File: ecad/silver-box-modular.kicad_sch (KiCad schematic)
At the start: 16 parts, among them J1 B6B-XH-A(LF)(SN), U1 CD4051BPWR4, U2 ESP32-DevKitC-V4-32D-custom-p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

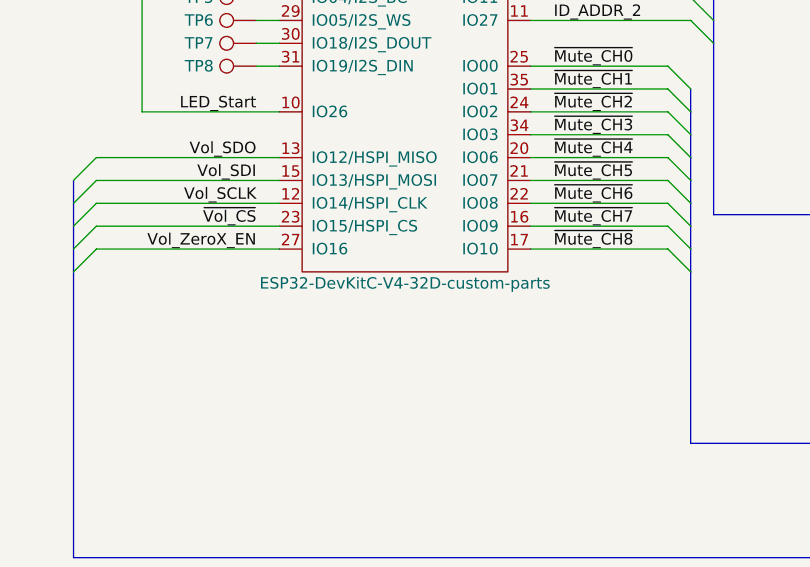
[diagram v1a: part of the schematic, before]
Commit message: Fixes to footprint numbering in multi-unit parts.
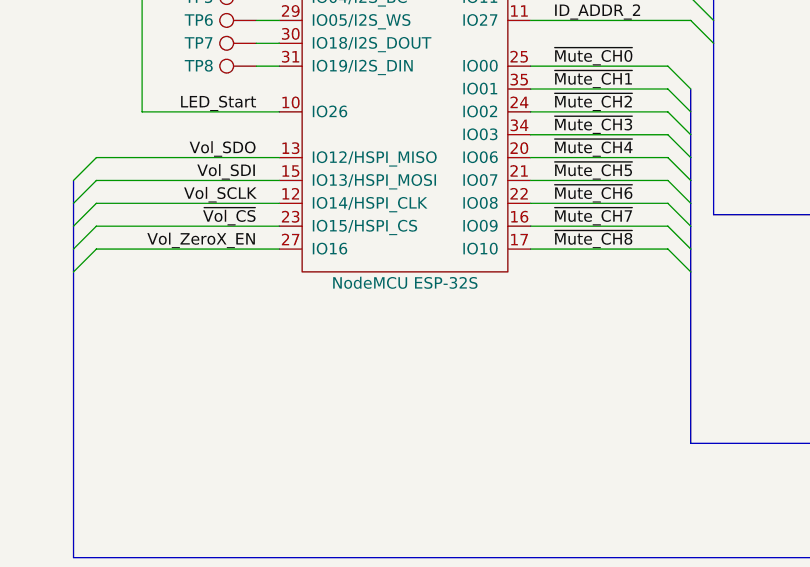
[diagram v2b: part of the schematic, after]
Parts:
- U2: value ESP32-DevKitC-V4-32D-custom-parts -> NodeMCU ESP-32S; footprint feetprints:ESP32-DevKitC-V4-32D -> silver-box-feetprints:NodeMCU ESP-32S
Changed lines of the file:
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@@
       (effects (font (size 1.27 1.27)))
     )
-    (property "Value" "ESP32-DevKitC-V4-32D-custom-parts" (at 148.59 177.8 0)
+    (property "Value" "NodeMCU ESP-32S" (at 148.59 177.8 0)
       (effects (font (size 1.27 1.27)))
     )
-    (property "Footprint" "feetprints:ESP32-DevKitC-V4-32D" (at 148.59 180.34 0)
+    (property "Footprint" "silver-box-feetprints:NodeMCU ESP-32S" (at 148.59 180.34 0)
       (effects (font (size 1.27 1.27)) hide)
     )
